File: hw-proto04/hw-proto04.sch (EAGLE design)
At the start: 27 parts, among them IC1 VN5E160MSTR-E, IC2 UCC27523DR, IC3 MCP2562T, J1 10, J2 10, Q1 SQJ147ELP-T1_GE3, Q2 SQJ147ELP-T1_GE3

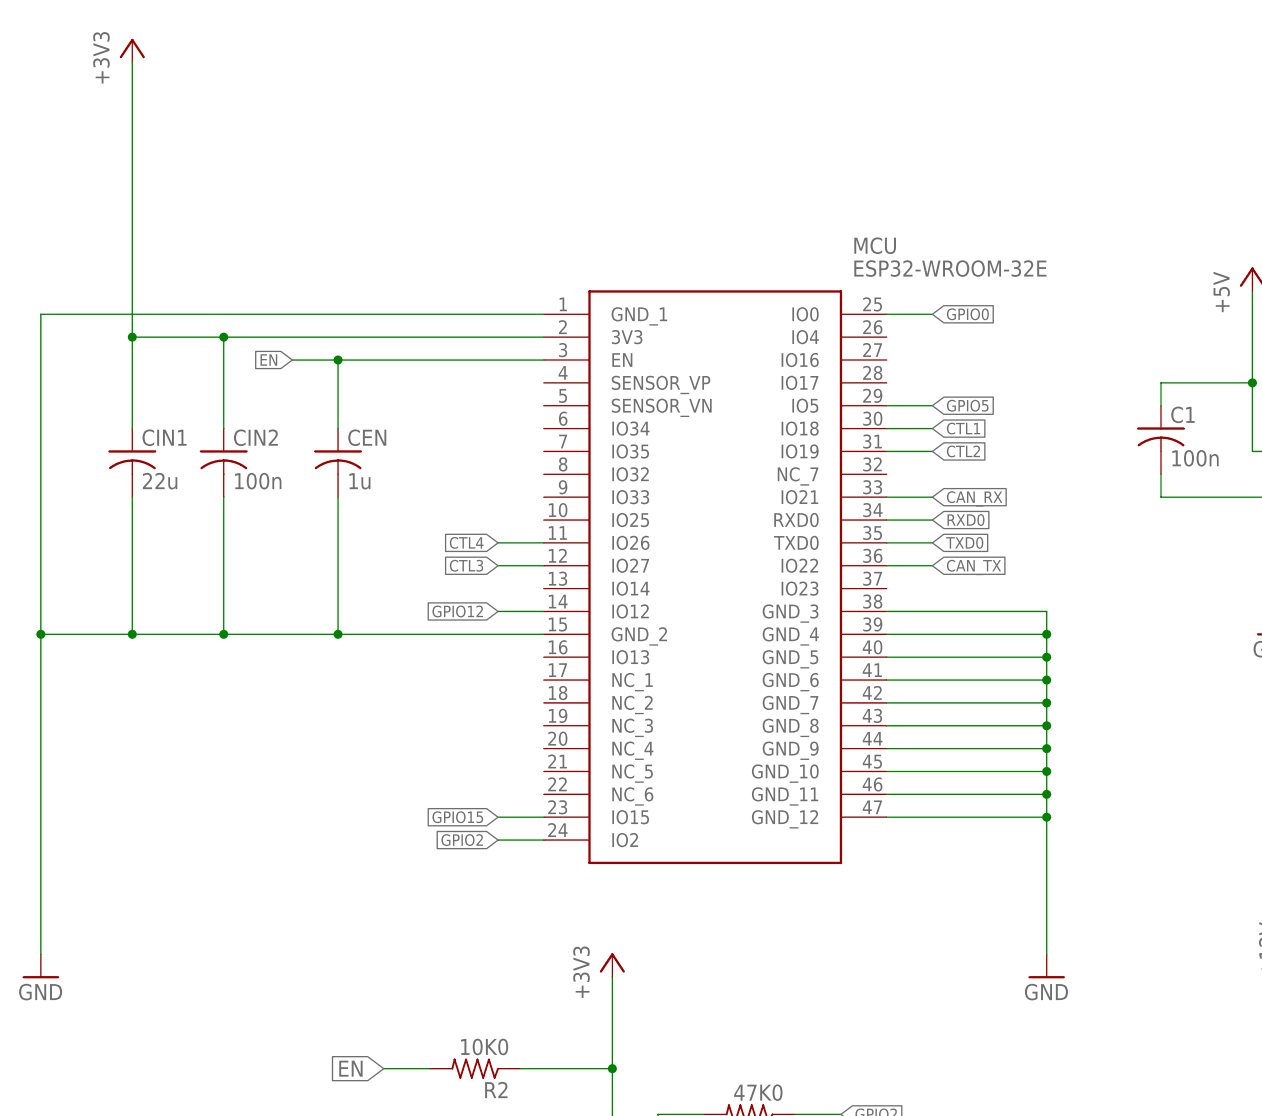
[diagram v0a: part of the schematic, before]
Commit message: swap esp32 for stm32
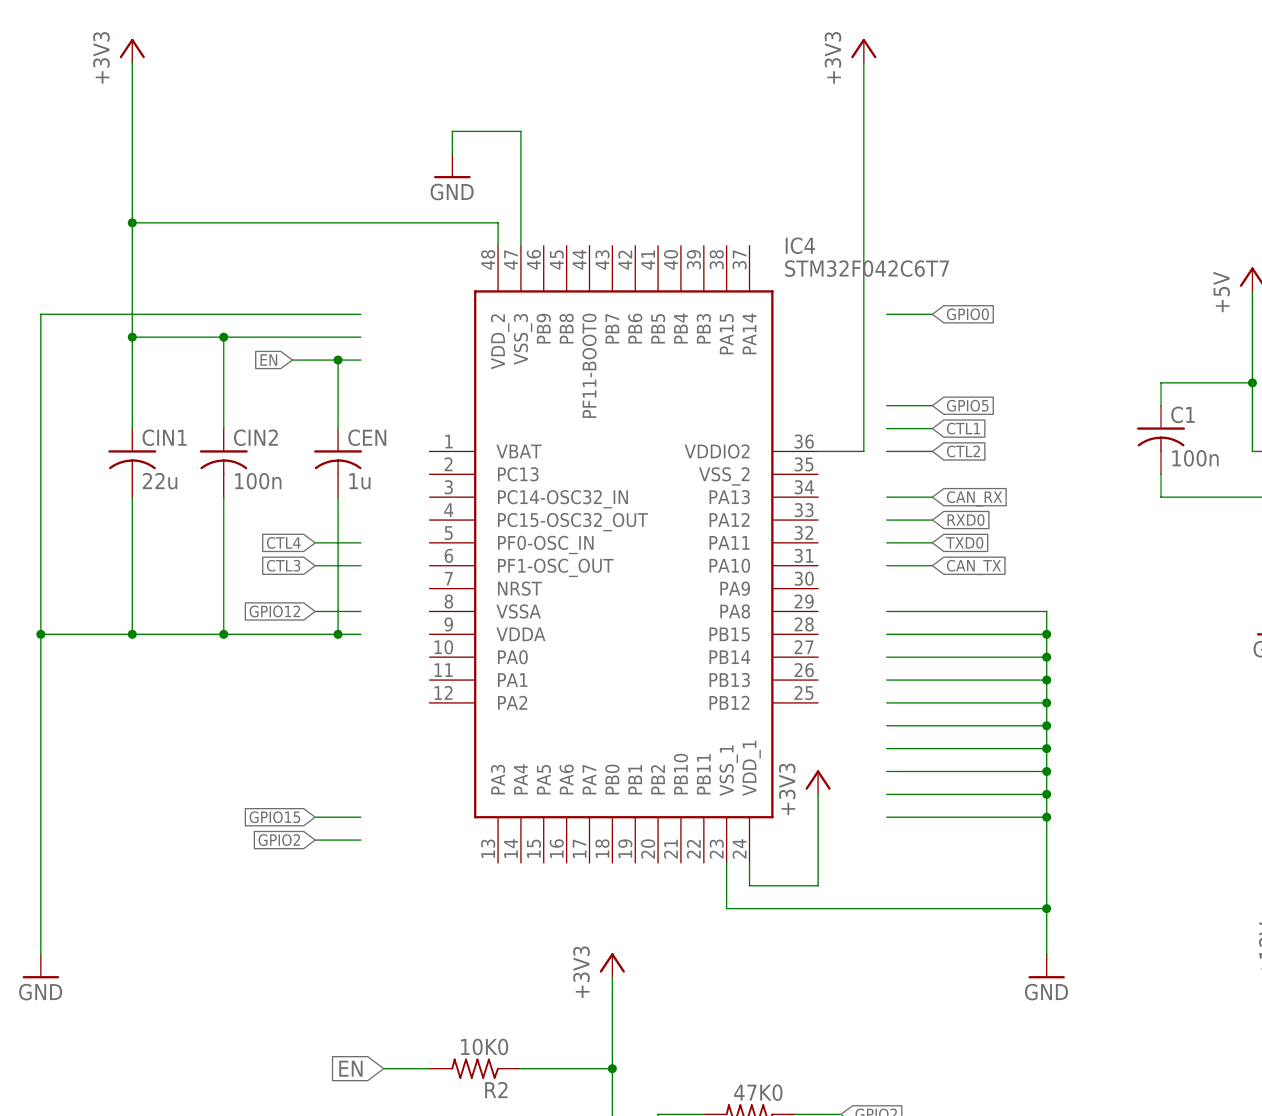
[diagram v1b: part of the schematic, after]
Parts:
- removed MCU: ESP32-WROOM-32E, ESP32-WROOM-32E-N8R2:ESP32-WROOM-32E-N8R2
- added IC4: STM32F042C6T7, STM32F042C6T7:STM32F042C6T7
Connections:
- removed net CTL4: MCU.IO26
- net +3V3: now also IC4.VDDIO2, IC4.VDD_1, IC4.VDD_2; no longer MCU.3V3
- net CAN_RX: no longer MCU.IO21
- net CAN_TX: no longer MCU.IO22
- net CTL1: no longer MCU.IO18
- net CTL2: no longer MCU.IO19
- net CTL3: no longer MCU.IO27
- net EN: no longer MCU.EN
- net GND: now also IC4.VSS_1, IC4.VSS_3; no longer MCU.GND_1, MCU.GND_10, MCU.GND_11, MCU.GND_12, MCU.GND_2, MCU.GND_3, MCU.GND_4, MCU.GND_5, MCU.GND_6, MCU.GND_7, MCU.GND_8, MCU.GND_9
- net GPIO0: no longer MCU.IO0
- net GPIO12: no longer MCU.IO12
- net GPIO15: no longer MCU.IO15
- net GPIO2: no longer MCU.IO2
- net GPIO5: no longer MCU.IO5
- net RXD0: no longer MCU.RXD0
- net TXD0: no longer MCU.TXD0

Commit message: work on new layout
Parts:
- removed VR3V3: +3V3, TSR_1-2433E:TSR_1-2433E
- added C3, C4, C5, C6: 1u, rcl:C-USC0603K
- added IC5: TLV74333PDBVR, TLV74333PDBVR:TLV74333PDBVR
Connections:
- net +12V: now also C5.1; no longer VR3V3.VIN+
- net +3V3: now also C4.1, IC5.OUT; no longer VR3V3.VOUT+
- net +5V: now also C3.1, C6.1, IC5.EN, IC5.IN
- net GND: now also C3.2, C4.2, C5.2, C6.2, IC5.GND; no longer VR3V3.GND
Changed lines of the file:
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@@
 <part name="GND4" library="supply1" deviceset="GND" device=""/>
 <part name="GND6" library="supply1" deviceset="GND" device=""/>
-<part name="VR3V3" library="TSR_1-2433E" deviceset="TSR_1-2433E" device="" value="+3V3"/>
 <part name="GND7" library="supply1" deviceset="GND" device=""/>
 <part name="+3V1" library="supply1" deviceset="+3V3" device=""/>
@@
 <part name="P+1" library="supply1" deviceset="+12V" device=""/>
 <part name="P+2" library="supply1" deviceset="+12V" device=""/>
-<part name="P+3" library="supply1" deviceset="+12V" device=""/>
 <part name="P+4" library="supply1" deviceset="+12V" device=""/>
 <part name="VR5V0" library="TSR_1-2433E" deviceset="TSR_1-2433E" device="" value="+5V"/>
@@
 <part name="+3V6" library="supply1" deviceset="+3V3" device=""/>
 <part name="GND12" library="supply1" deviceset="GND" device=""/>
+<part name="IC5" library="TLV74333PDBVR" deviceset="TLV74333PDBVR" device=""/>
+<part name="P+3" library="supply1" deviceset="+5V" device=""/>
+<part name="C3" library="rcl" deviceset="C-US" device="C0603K" value="1u"/>
+<part name="C4" library="rcl" deviceset="C-US" device="C0603K" value="1u"/>
+<part name="C5" library="rcl" deviceset="C-US" device="C0603K" value="1u"/>
+<part name="C6" library="rcl" deviceset="C-US" device="C0603K" value="1u"/>
 </parts>
 <sheets>
@@
 <instance part="GND4" gate="1" x="132.08" y="73.66"/>
 <instance part="GND6" gate="1" x="76.2" y="190.5"/>
-<instance part="VR3V3" gate="G$1" x="165.1" y="144.78" rot="R90"/>
-<instance part="GND7" gate="1" x="167.64" y="127"/>
-<instance part="+3V1" gate="G$1" x="193.04" y="157.48"/>
+<instance part="GND7" gate="1" x="147.32" y="127"/>
+<instance part="+3V1" gate="G$1" x="200.66" y="170.18"/>
 <instance part="+3V2" gate="G$1" x="-50.8" y="256.54"/>
 <instance part="P+1" gate="1" x="-10.16" y="93.98"/>
 <instance part="P+2" gate="1" x="132.08" y="109.22"/>
-<instance part="P+3" gate="1" x="144.78" y="154.94"/>
 <instance part="P+4" gate="1" x="78.74" y="157.48"/>
 <instance part="VR5V0" gate="G$1" x="96.52" y="144.78" rot="R90"/>
-<instance part="GND8" gate="1" x="99.06" y="129.54"/>
+<instance part="GND8" gate="1" x="99.06" y="121.92"/>
 <instance part="P+5" gate="1" x="119.38" y="157.48"/>
 <instance part="+3V4" gate="G$1" x="142.24" y="231.14"/>
@@
 <instance part="+3V6" gate="G$1" x="30.48" y="256.54"/>
 <instance part="GND12" gate="1" x="-15.24" y="241.3"/>
+<instance part="IC5" gate="G$1" x="154.94" y="160.02"/>
+<instance part="P+3" gate="1" x="139.7" y="170.18"/>
+<instance part="C3" gate="G$1" x="139.7" y="147.32"/>
+<instance part="C4" gate="G$1" x="187.96" y="147.32"/>
+<instance part="C5" gate="G$1" x="78.74" y="137.16"/>
+<instance part="C6" gate="G$1" x="119.38" y="137.16"/>
 </instances>
 <busses>
@@
 </segment>
 <segment>
-<pinref part="VR3V3" gate="G$1" pin="GND"/>
-<pinref part="GND7" gate="1" pin="GND"/>
-<wire x1="167.64" y1="144.78" x2="167.64" y2="129.54" width="0.1524" layer="91"/>
-</segment>
-<segment>
 <pinref part="VR5V0" gate="G$1" pin="GND"/>
 <pinref part="GND8" gate="1" pin="GND"/>
-<wire x1="99.06" y1="144.78" x2="99.06" y2="132.08" width="0.1524" layer="91"/>
+<wire x1="99.06" y1="144.78" x2="99.06" y2="129.54" width="0.1524" layer="91"/>
+<pinref part="C5" gate="G$1" pin="2"/>
+<wire x1="99.06" y1="129.54" x2="99.06" y2="124.46" width="0.1524" layer="91"/>
+<wire x1="99.06" y1="129.54" x2="78.74" y2="129.54" width="0.1524" layer="91"/>
+<wire x1="78.74" y1="129.54" x2="78.74" y2="132.08" width="0.1524" layer="91"/>
+<junction x="99.06" y="129.54"/>
+<pinref part="C6" gate="G$1" pin="2"/>
+<wire x1="99.06" y1="129.54" x2="119.38" y2="129.54" width="0.1524" layer="91"/>
+<wire x1="119.38" y1="129.54" x2="119.38" y2="132.08" width="0.1524" layer="91"/>
 </segment>
 <segment>
@@
 <wire x1="-15.24" y1="246.38" x2="-15.24" y2="243.84" width="0.1524" layer="91"/>
 <pinref part="GND12" gate="1" pin="GND"/>
+</segment>
+<segment>
+<pinref part="IC5" gate="G$1" pin="GND"/>
+<pinref part="GND7" gate="1" pin="GND"/>
+<wire x1="154.94" y1="157.48" x2="147.32" y2="157.48" width="0.1524" layer="91"/>
+<wire x1="147.32" y1="157.48" x2="147.32" y2="139.7" width="0.1524" layer="91"/>
+<pinref part="C3" gate="G$1" pin="2"/>
+<wire x1="147.32" y1="139.7" x2="147.32" y2="129.54" width="0.1524" layer="91"/>
+<wire x1="147.32" y1="139.7" x2="139.7" y2="139.7" width="0.1524" layer="91"/>
+<wire x1="139.7" y1="139.7" x2="139.7" y2="142.24" width="0.1524" layer="91"/>
+<junction x="147.32" y="139.7"/>
+<pinref part="C4" gate="G$1" pin="2"/>
+<wire x1="147.32" y1="139.7" x2="187.96" y2="139.7" width="0.1524" layer="91"/>
+<wire x1="187.96" y1="139.7" x2="187.96" y2="142.24" width="0.1524" layer="91"/>
 </segment>
 </net>
@@
 <net name="+3V3" class="0">
 <segment>
-<pinref part="VR3V3" gate="G$1" pin="VOUT+"/>
-<wire x1="170.18" y1="144.78" x2="170.18" y2="142.24" width="0.1524" layer="91"/>
-<pinref part="+3V1" gate="G$1" pin="+3V3"/>
-<wire x1="170.18" y1="142.24" x2="193.04" y2="142.24" width="0.1524" layer="91"/>
-<wire x1="193.04" y1="142.24" x2="193.04" y2="154.94" width="0.1524" layer="91"/>
-</segment>
-<segment>
 <pinref part="+3V2" gate="G$1" pin="+3V3"/>
 <wire x1="-25.4" y1="223.52" x2="-40.64" y2="223.52" width="0.1524" layer="91"/>
@@
 <wire x1="30.48" y1="210.82" x2="30.48" y2="254" width="0.1524" layer="91"/>
 <pinref part="+3V6" gate="G$1" pin="+3V3"/>
+</segment>
+<segment>
+<pinref part="IC5" gate="G$1" pin="OUT"/>
+<pinref part="+3V1" gate="G$1" pin="+3V3"/>
+<wire x1="180.34" y1="157.48" x2="187.96" y2="157.48" width="0.1524" layer="91"/>
+<wire x1="187.96" y1="157.48" x2="200.66" y2="157.48" width="0.1524" layer="91"/>
+<wire x1="200.66" y1="157.48" x2="200.66" y2="167.64" width="0.1524" layer="91"/>
+<pinref part="C4" gate="G$1" pin="1"/>
+<wire x1="187.96" y1="149.86" x2="187.96" y2="157.48" width="0.1524" layer="91"/>
+<junction x="187.96" y="157.48"/>
 </segment>
 </net>
@@
 </segment>
 <segment>
-<wire x1="144.78" y1="152.4" x2="144.78" y2="142.24" width="0.1524" layer="91"/>
-<pinref part="VR3V3" gate="G$1" pin="VIN+"/>
-<wire x1="144.78" y1="142.24" x2="165.1" y2="142.24" width="0.1524" layer="91"/>
-<wire x1="165.1" y1="142.24" x2="165.1" y2="144.78" width="0.1524" layer="91"/>
-<pinref part="P+3" gate="1" pin="+12V"/>
-</segment>
-<segment>
 <pinref part="VR5V0" gate="G$1" pin="VIN+"/>
 <wire x1="96.52" y1="144.78" x2="96.52" y2="142.24" width="0.1524" layer="91"/>
@@
 <wire x1="96.52" y1="142.24" x2="78.74" y2="142.24" width="0.1524" layer="91"/>
 <wire x1="78.74" y1="142.24" x2="78.74" y2="154.94" width="0.1524" layer="91"/>
+<pinref part="C5" gate="G$1" pin="1"/>
+<wire x1="78.74" y1="139.7" x2="78.74" y2="142.24" width="0.1524" layer="91"/>
+<junction x="78.74" y="142.24"/>
 </segment>
 <segment>
@@
 <wire x1="101.6" y1="142.24" x2="119.38" y2="142.24" width="0.1524" layer="91"/>
 <wire x1="119.38" y1="142.24" x2="119.38" y2="154.94" width="0.1524" layer="91"/>
+<pinref part="C6" gate="G$1" pin="1"/>
+<wire x1="119.38" y1="139.7" x2="119.38" y2="142.24" width="0.1524" layer="91"/>
+<junction x="119.38" y="142.24"/>
 </segment>
 <segment>
@@
 <junction x="73.66" y="218.44"/>
 </segment>
-</net>
+<segment>
+<pinref part="IC5" gate="G$1" pin="IN"/>
+<pinref part="P+3" gate="1" pin="+5V"/>
+<wire x1="154.94" y1="160.02" x2="139.7" y2="160.02" width="0.1524" layer="91"/>
+<wire x1="139.7" y1="160.02" x2="139.7" y2="167.64" width="0.1524" layer="91"/>
+<pinref part="IC5" gate="G$1" pin="EN"/>
+<wire x1="154.94" y1="154.94" x2="139.7" y2="154.94" width="0.1524" layer="91"/>
+<wire x1="139.7" y1="154.94" x2="139.7" y2="160.02" width="0.1524" layer="91"/>
+<junction x="139.7" y="160.02"/>
+<pinref part="C3" gate="G$1" pin="1"/>
+<wire x1="139.7" y1="154.94" x2="139.7" y2="149.86" width="0.1524" layer="91"/>
+<junction x="139.7" y="154.94"/>
+</segment>
+</net>

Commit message: schematic updates
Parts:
- removed CEN: 1u, rcl:C-USC0603K
- removed CIN1: 22u, rcl:C-USC0805K
- removed CIN2: 100n, rcl:C-USC0603K
- added CNRST, CVDD1, CVDDIO, VDD2: 100n, rcl:C-USC0603K
- added CVDD, CVDDIO2: 4u7, rcl:C-USC0603K
- added CVDDA1: 10n, rcl:C-USC0603K
- added CVDDA2: 1u, rcl:C-USC0603K
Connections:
- new net N$8: CNRST.1, IC4.NRST
- net +3V3: now also CVDD.1, CVDD1.1, CVDDA1.1, CVDDA2.1, CVDDIO.1, CVDDIO2.1, IC4.VDDA, VDD2.1; no longer CIN1.1, CIN2.1
- net EN: no longer CEN.1
- net GND: now also CNRST.2, CVDD.2, CVDD1.2, CVDDA1.2, CVDDA2.2, CVDDIO.2, CVDDIO2.2, IC4.VSSA, IC4.VSS_2, VDD2.2; no longer CEN.2, CIN1.2, CIN2.2

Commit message: schematic updates
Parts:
- removed CVDDA1: 10n, rcl:C-USC0603K
- removed CVDDA2: 1u, rcl:C-USC0603K
- removed R2: 10K0, rcl:R-US_R0603
- removed R3, R4, R5, R6, R7: 47K0, rcl:R-US_R0603
- removed VDD2: 100n, rcl:C-USC0603K
- added CVDA1: 10n, rcl:C-USC0603K
- added CVDA2: 1u, rcl:C-USC0603K
- added CVDD2: 100n, rcl:C-USC0603K
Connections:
- removed net GPIO12: R5.1
- removed net GPIO15: R3.2
- removed net GPIO2: R6.1
- removed net GPIO5: R7.2
- new net CAN_RX_ALT: IC4.PB8
- new net CAN_TX_ALT: IC4.PB9
- new net RX: IC4.PA10
- new net TX: IC4.PA9
- net +3V3: now also CVDA1.1, CVDA2.1, CVDD2.1; no longer CVDDA1.1, CVDDA2.1, R2.1, R3.1, R4.1, R7.1, VDD2.1
- net CAN_RX: now also IC4.PA11
- net CAN_TX: now also IC4.PA12
- net EN: no longer R2.2
- net GND: now also CVDA1.2, CVDA2.2, CVDD2.2; no longer CVDDA1.2, CVDDA2.2, R5.2, R6.2, VDD2.2
- net GPIO0: no longer R4.2
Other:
- moved on the sheet: CVDD, CVDD1, CVDDIO, CVDDIO2

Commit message: layout, routing and schematic refinement
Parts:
- removed C3, C4, C5, C6: 1u, rcl:C-USC0603K
- removed PROG: 1X5, adafruit:1X5
- added C3V1, C3V2, C5V1, C5V2: 1u, rcl:C-USC0603K
- added PRG, SER: (no value), SparkFun-Connectors:M04LOCK
- renumbered C1 to CCAN1, C2 to CCAN2
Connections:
- removed net EN: PROG.3
- removed net GPIO0: PROG.4
- removed net RX: IC4.PA10
- removed net RXD0: PROG.2
- removed net TX: IC4.PA9
- removed net TXD0: PROG.1
- new net RX1: IC4.PA10, SER.3
- new net SWCLK: IC4.PB2, PRG.3
- new net SWDIO: IC4.PB1, PRG.2
- new net TX1: IC4.PA9, SER.2
- net +12V: now also C5V1.1; no longer C5.1
- net +3V3: now also C3V2.1, PRG.1, SER.4; no longer C4.1
- net +5V: now also C3V1.1, C5V2.1; no longer C3.1, C6.1
- net CTL1: now also IC4.PB3
- net CTL2: now also IC4.PB4
- net CTL3: now also IC4.PA13
- net GND: now also C3V1.2, C3V2.2, C5V1.2, C5V2.2, PRG.4, SER.1; no longer C3.2, C4.2, C5.2, C6.2, PROG.5
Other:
- moved on the sheet: CAN-1, CAN-2, CAN-3, CNRST, IC1, IC5, PWR, R1, VR5V0
